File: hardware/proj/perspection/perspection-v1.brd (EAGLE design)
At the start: 90 x 70 mm, 274 parts, among them J1 MICRO-USB-10118192-0001LF, J10 1X5, J11 1X4, J2 1X6-PTSA_1.5/6-3.5-Z, J3 1X2-PTSA_1.5/2-3.5-Z, J4 1X2-JST-PH-SMD, J5 1X2-0428202213, J6 JTAG-ARM_TC-10, J7 JTAG-ARM_TC-10, J8 1X3-0.1IN_THRUHOLE, J9 1X2-PTSA_1.5/2-3.5-Z, Q1 NMOS-CSD18533Q5A, Q10 NMOS-CSD18533Q5A, Q11 IRFML8244TRPBF, Q2 NMOS-CSD18533Q5A, Q3 NMOS-CSD18533Q5A, Q4 NMOS-CSD18533Q5A, Q5 NMOS-CSD18533Q5A, Q6 NMOS-CSD18533Q5A, Q7 NMOS-CSD18533Q5A, Q8 BSS138L, Q9 BSS138L, U1 ATUM, U10 DRV8301DCAR, U11 OPA2374AIDCNR, U12 OPA170AIDBVR, U13 BNO055, U14 TPS81256, U2 FT232RQ, U3 TPS79933DDCR, U4 MCP73831T-2ACI/OT, U5 TMS320F28069MPZT, U6 DRV8801PWPR, U7 DRV8801PWPR, U8 DRV8801PWPR, U9 DRV8801PWPR, Y1 32.768kHz

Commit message: fixed fuckups sorry bros
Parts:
- moved R40 20.0 mm to (23.9, 19.7), turned to 90 degrees
- moved R114 1.92 mm to (25.5, 18.3), turned to 180 degrees
- moved R104 0.60 mm to (42.1, 25.4)
- moved R113 0.28 mm to (23.8, 18.3)
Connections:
- removed net _!FAULT: R40.2, U5.88
- new net N$52: R40.2, U5.50
- net N$21: now also U5.97; no longer U5.50
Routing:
- net !FAULT: track 19.1 -> 48.3 mm, vias 4 -> 8
- net N$21: track 29.4 -> 5.76 mm, vias 4 -> 2
- net N$51: track 74.6 -> 53.4 mm
- net ENABLE2: track 25.4 -> 23.0 mm
- net _!FAULT: track 1.85 -> 0.00 mm
- net N$50: track 42.9 -> 44.7 mm
- net _SPI_MOSI: track 29.2 -> 30.7 mm
- net N$52: track 0.00 -> 1.26 mm
- net _SPI_SCK: track 35.4 -> 34.2 mm
- net AUX_ENABLE: track 74.0 -> 74.8 mm
- net PWM_BL: track 47.6 -> 48.4 mm
- net N$44: track 1.85 -> 1.25 mm

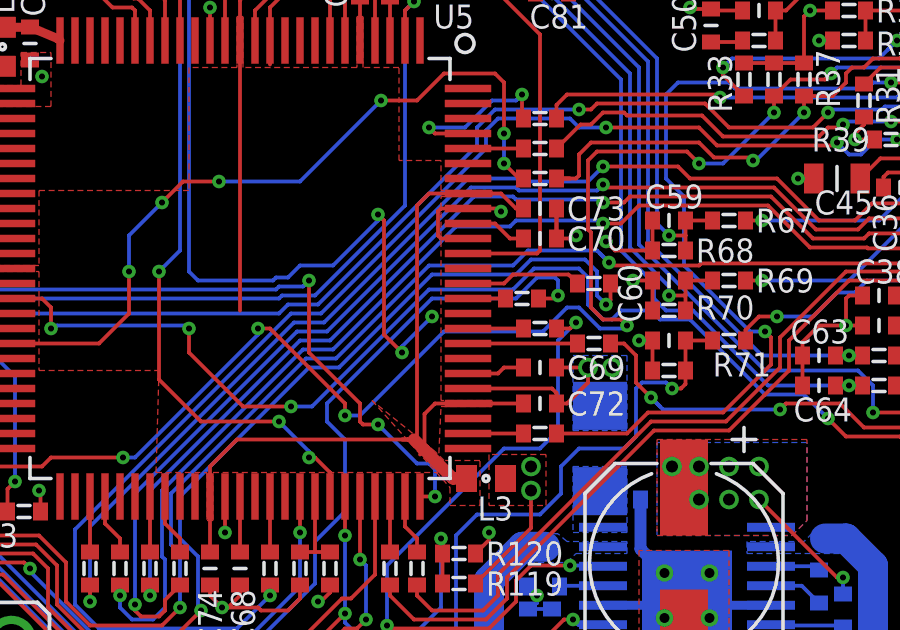
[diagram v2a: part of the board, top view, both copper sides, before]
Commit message: fixed stub (!!), set resistor values for LED driver and updated part numbers accordingly
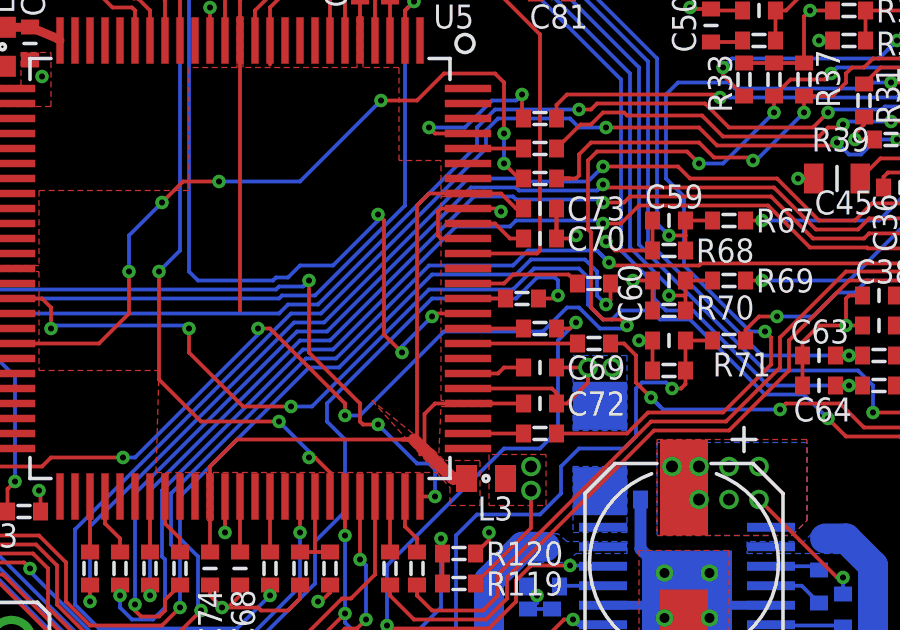
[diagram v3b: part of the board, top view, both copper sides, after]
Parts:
- R79: value (none) -> 0.68
- R82: value (none) -> 470k
- VR1: value 200k -> 10k
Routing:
- net _SPI_SCK: track 34.2 -> 35.3 mm
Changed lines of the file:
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@@
 <layers>
 <layer number="1" name="Top" color="4" fill="1" visible="yes" active="yes"/>
-<layer number="2" name="Route2" color="11" fill="3" visible="yes" active="yes"/>
+<layer number="2" name="Route2" color="11" fill="3" visible="no" active="yes"/>
 <layer number="3" name="Route3" color="4" fill="3" visible="no" active="no"/>
 <layer number="4" name="Route4" color="1" fill="4" visible="no" active="no"/>
@@
 <attribute name="MFG_PN" value="MX3SWT-A1-0000-000CE5" x="113.27" y="-1.14" size="1.778" layer="27" display="off"/>
 </element>
-<element name="R79" library="perspection" package="R0805" value="" x="31.8" y="45.1" smashed="yes" rot="R90">
+<element name="R79" library="perspection" package="R0805" value="0.68" x="31.8" y="45.1" smashed="yes" rot="R90">
 <attribute name="MFG_NAME" value="" x="105.46" y="71.77" size="1.778" layer="27" rot="R90" display="off"/>
 <attribute name="DIST_NAME" value="" x="105.46" y="71.77" size="1.778" layer="27" rot="R90" display="off"/>
@@
 <attribute name="NAME" x="33.2" y="45.1" size="0.5" layer="37" font="vector" ratio="15" rot="R270" align="center"/>
 </element>
-<element name="R82" library="perspection" package="R0402" value="" x="21" y="40.1" smashed="yes" rot="R270">
+<element name="R82" library="perspection" package="R0402" value="470k" x="21" y="40.1" smashed="yes" rot="R270">
 <attribute name="MFG_NAME" value="" x="-75.52" y="-5.62" size="1.778" layer="27" rot="R270" display="off"/>
 <attribute name="DIST_NAME" value="" x="-75.52" y="-5.62" size="1.778" layer="27" rot="R270" display="off"/>
@@
 <attribute name="NAME" x="21" y="40.1" size="0.5" layer="37" font="vector" ratio="15" rot="R270" align="center"/>
 </element>
-<element name="VR1" library="perspection" package="ST-4EA" value="200k" x="24.5" y="41.4" smashed="yes" rot="R270">
+<element name="VR1" library="perspection" package="ST-4EA" value="10k" x="24.5" y="41.4" smashed="yes" rot="R270">
 <attribute name="MFG_NAME" value="Copal Electronics Inc." x="-37.73" y="-13.21" size="1.778" layer="27" rot="R270" display="off"/>
 <attribute name="DIST_NAME" value="Digi-Key" x="-37.73" y="-13.21" size="1.778" layer="27" rot="R270" display="off"/>
-<attribute name="DIST_PN" value="ST4ETA204CT-ND" x="-37.73" y="-13.21" size="1.778" layer="27" rot="R270" display="off"/>
-<attribute name="MFG_PN" value="ST4ETA204" x="-37.73" y="-13.21" size="1.778" layer="27" rot="R270" display="off"/>
+<attribute name="DIST_PN" value="ST4ETA103CT-ND" x="-37.73" y="-13.21" size="1.778" layer="27" rot="R270" display="off"/>
+<attribute name="MFG_PN" value="ST4ETA103" x="-37.73" y="-13.21" size="1.778" layer="27" rot="R270" display="off"/>
 <attribute name="NAME" x="24.5" y="41.4" size="0.8" layer="37" font="vector" ratio="15" rot="R270" align="center"/>
 <attribute name="NAME" x="23.4" y="41" size="0.8" layer="25" font="vector" ratio="15"/>
@@
 <via x="38.1" y="23.6" extent="1-16" drill="0.2"/>
 <via x="39.1" y="24.8" extent="1-16" drill="0.2"/>
-<wire x1="39.1" y1="24.8" x2="39.2" y2="24.9" width="0.127" layer="1"/>
 <wire x1="33.9" y1="26.1" x2="34.3" y2="26.1" width="0.127" layer="16"/>
 <wire x1="34.3" y1="26.1" x2="34.7" y2="26.5" width="0.127" layer="16"/>
@@
 <wire x1="37.5" y1="24.2" x2="37.5" y2="28" width="0.127" layer="1"/>
 <wire x1="37.5" y1="28" x2="37.3" y2="28.2" width="0.127" layer="1"/>
-<wire x1="39.2" y1="24.9" x2="40.3" y2="24.9" width="0" layer="19" extent="1-1"/>
+<wire x1="40.3" y1="24.9" x2="39.2" y2="24.9" width="0.127" layer="1"/>
+<wire x1="39.2" y1="24.9" x2="39.1" y2="24.8" width="0.127" layer="1"/>
 </signal>
 <signal name="_SPI_MISO" class="1">
